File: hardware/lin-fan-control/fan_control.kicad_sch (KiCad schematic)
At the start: 28 parts, among them J4 FAN, J5 TRANS, Q3 2N7002, Q4 SUD50P04-08, U10 LM555xMM, U11 74LVC1G14, U6 74LVC1G14, U7 LMH6611, U8 LM96163CISD/NOPB, U9 74LVC1G14

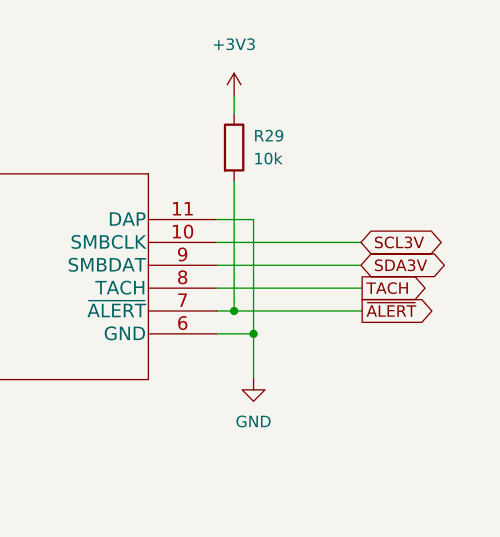
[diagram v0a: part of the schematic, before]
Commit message: Update the schematics... remove PCA9536, use voltage regulator
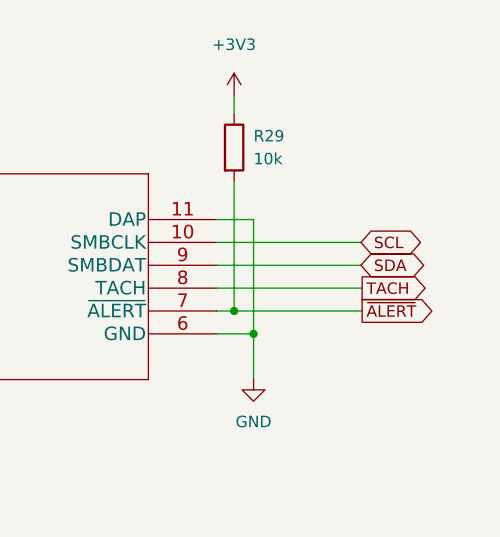
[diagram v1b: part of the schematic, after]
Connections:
- net SCL3V renamed SCL
- net SDA3V renamed SDA
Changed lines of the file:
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@@
   (title_block
     (title "LINBus Fan Controller")
-    (date "2023-02-19")
+    (date "2023-03-03")
     (rev "1.0")
     (company "Gavin Hurlbut")
@@
     )
   )
-  (global_label "SCL3V" (shape bidirectional) (at 241.554 49.53 0) (fields_autoplaced)
+  (global_label "SCL" (shape bidirectional) (at 241.554 49.53 0) (fields_autoplaced)
     (effects (font (size 1.27 1.27)) (justify left))
-    (property "Intersheet References" "${INTERSHEET_REFS}" (id 0) (at 249.6839 49.4506 0)
+    (property "Intersheet References" "${INTERSHEET_REFS}" (id 0) (at 247.3858 49.4506 0)
       (effects (font (size 1.27 1.27)) (justify left) hide)
     )
@@
     )
   )
-  (global_label "SDA3V" (shape bidirectional) (at 241.554 52.07 0) (fields_autoplaced)
+  (global_label "SDA" (shape bidirectional) (at 241.554 52.07 0) (fields_autoplaced)
     (effects (font (size 1.27 1.27)) (justify left))
-    (property "Intersheet References" "${INTERSHEET_REFS}" (id 0) (at 249.7444 51.9906 0)
+    (property "Intersheet References" "${INTERSHEET_REFS}" (id 0) (at 247.4463 51.9906 0)
       (effects (font (size 1.27 1.27)) (justify left) hide)
     )
